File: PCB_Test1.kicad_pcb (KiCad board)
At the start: 2 copper layers, 8 parts, among them IC101 L70REL-M37-EIT, Q101 DTC143Z

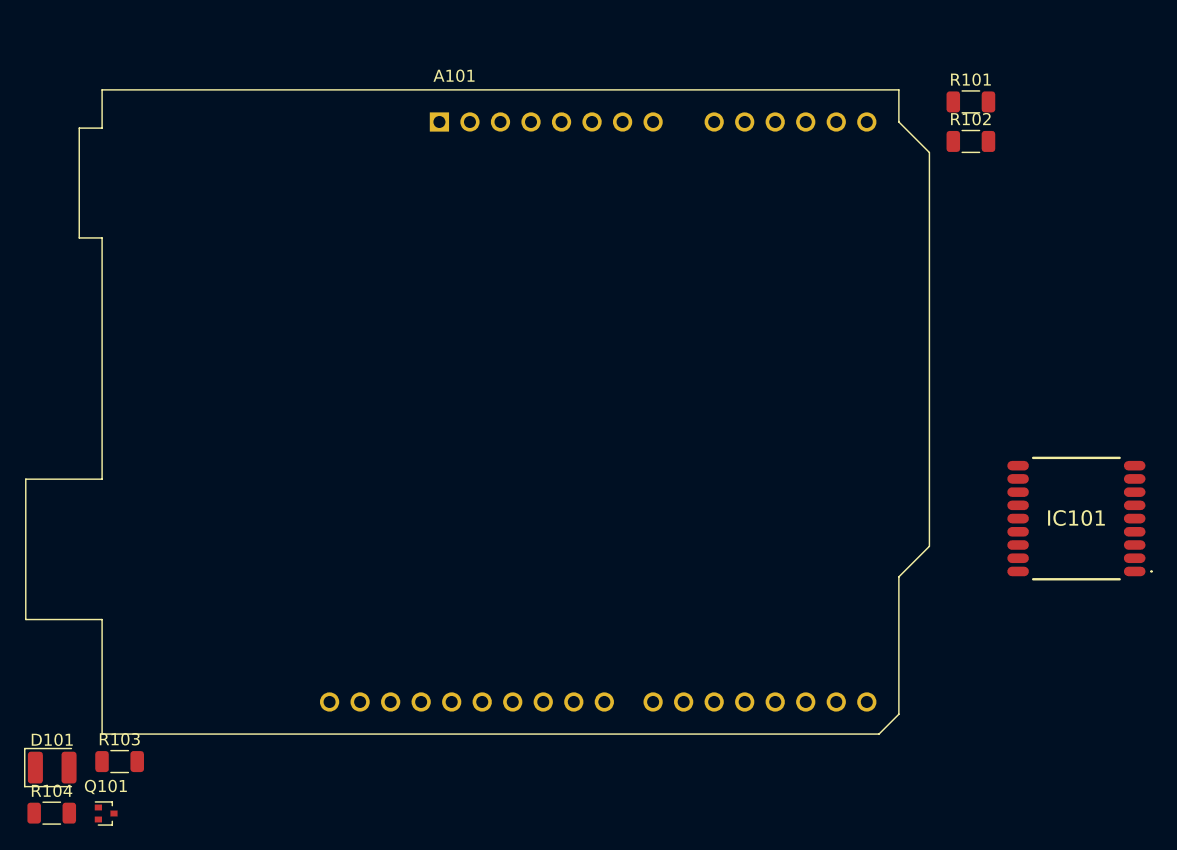
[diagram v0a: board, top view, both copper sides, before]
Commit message: Added male headers for arduino uno r3
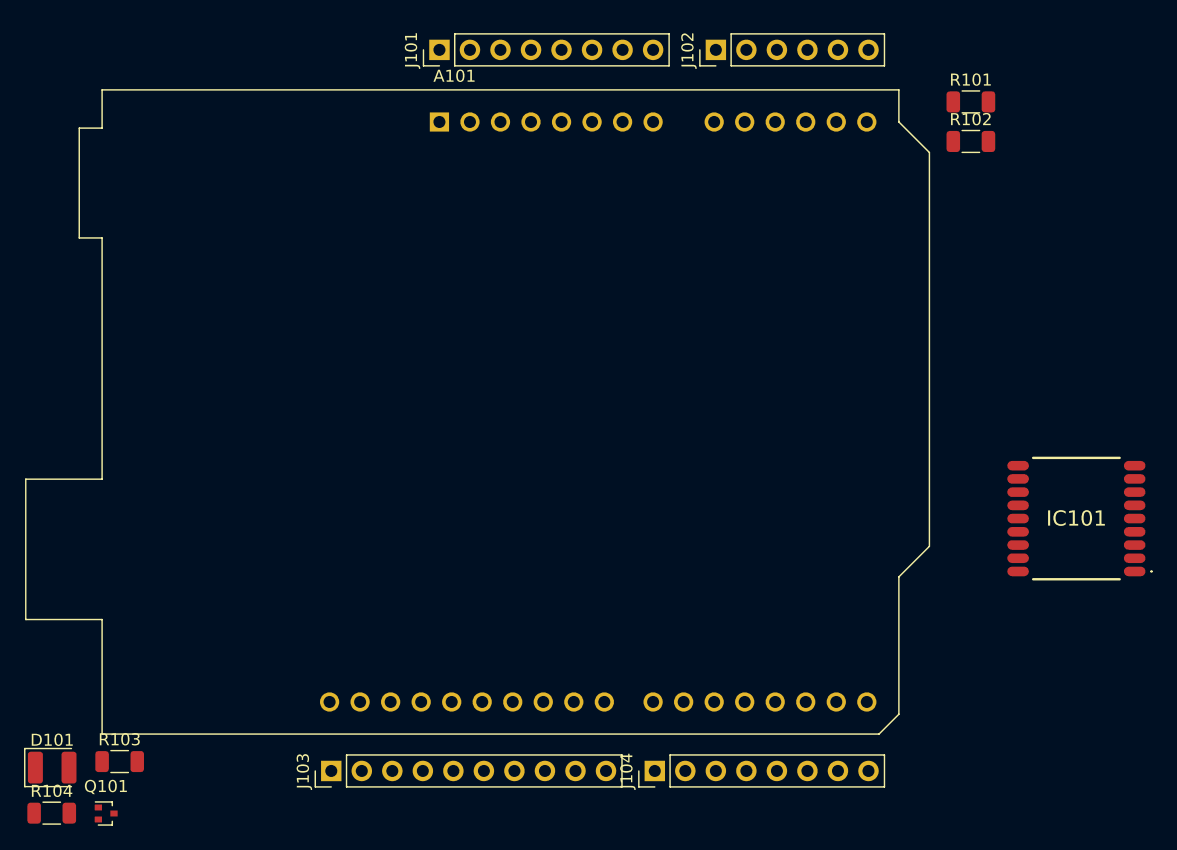
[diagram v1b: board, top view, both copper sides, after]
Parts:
- added J101: Conn_01x08_Male, Connector_PinHeader_2.54mm:PinHeader_1x08_P2.54mm_Vertical, F.Cu at (148.0, 51.0)
- added J102: Conn_01x06_Male, Connector_PinHeader_2.54mm:PinHeader_1x06_P2.54mm_Vertical, F.Cu at (171.0, 51.0)
- added J103: Conn_01x10_Male, Connector_PinHeader_2.54mm:PinHeader_1x10_P2.54mm_Vertical, F.Cu at (139.0, 111.0)
- added J104: Conn_01x08_Male, Connector_PinHeader_2.54mm:PinHeader_1x08_P2.54mm_Vertical, F.Cu at (165.9, 111.0)
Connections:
- net VCC renamed +3V3
